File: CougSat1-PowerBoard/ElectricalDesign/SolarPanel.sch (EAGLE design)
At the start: 120 parts, among them J101 Wire Harness Connector, U1 INA199C2, U100 SPV1040, U101 SPV1040, U2 INA199C2, U3 INA199C2, U4 INA199C2, U5 AD7291, U6 AD7291, U7 AD8515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

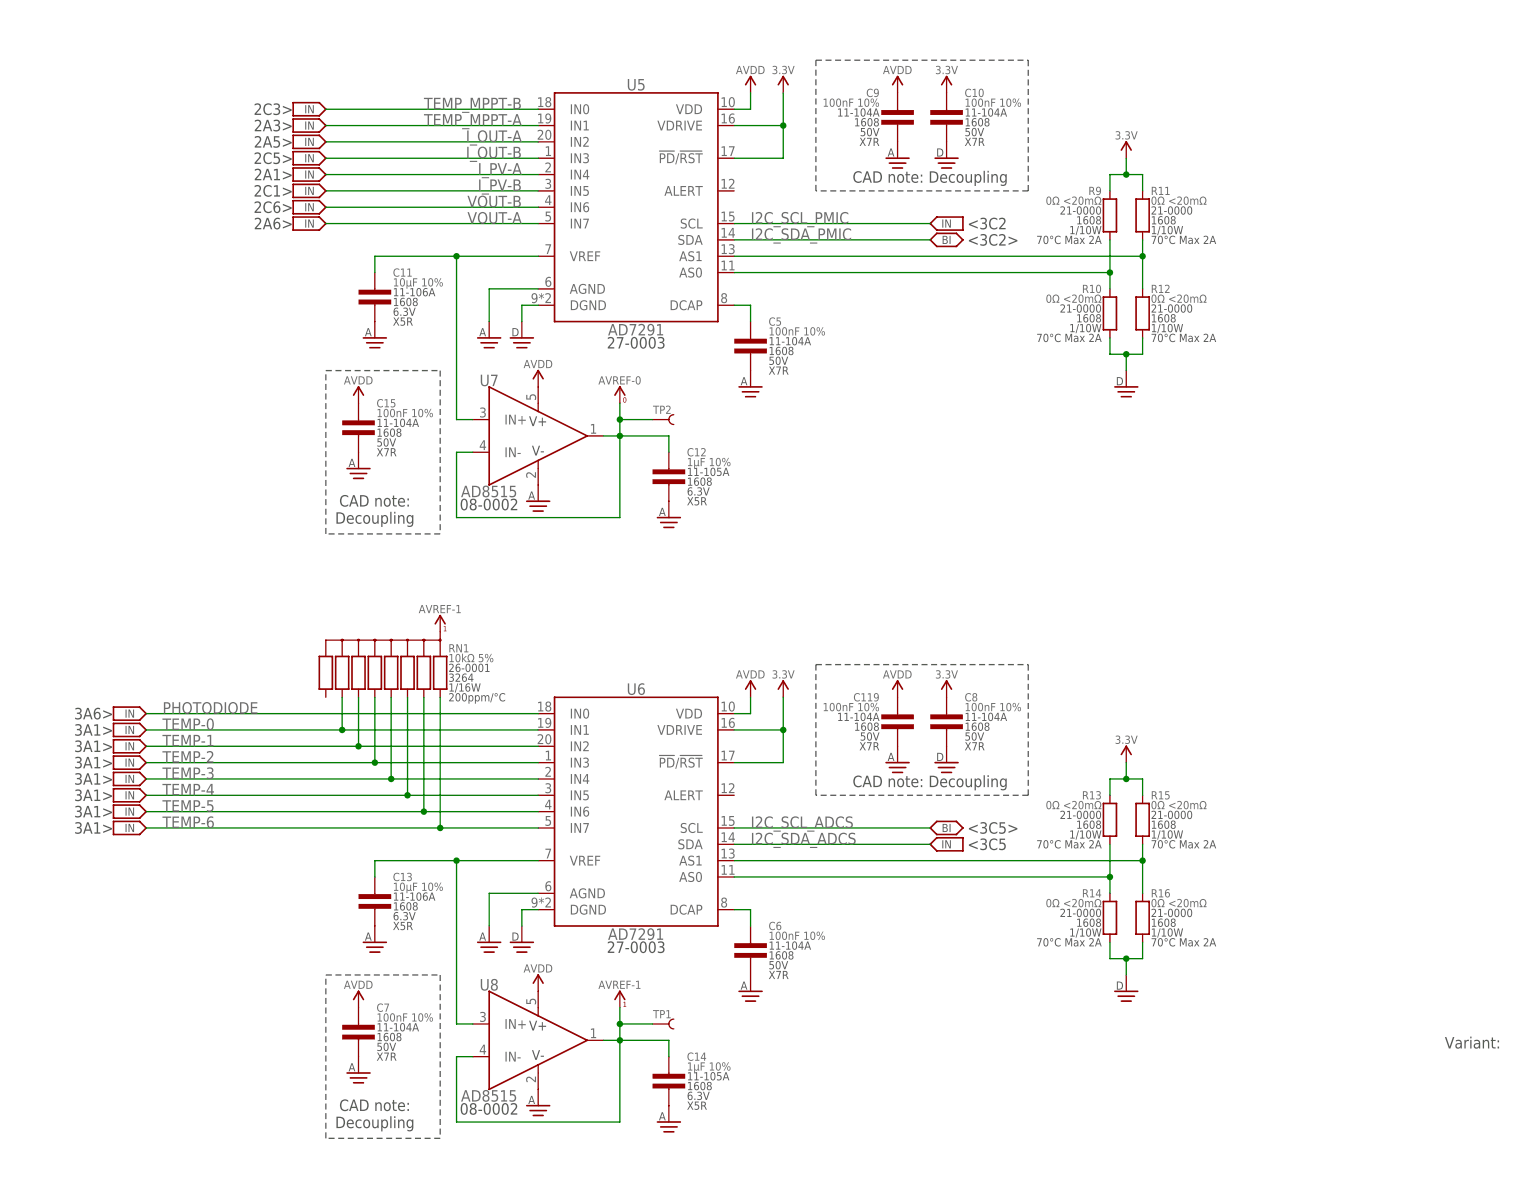
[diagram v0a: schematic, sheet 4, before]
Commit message: Stuffed addresses on variants, exported PDFs
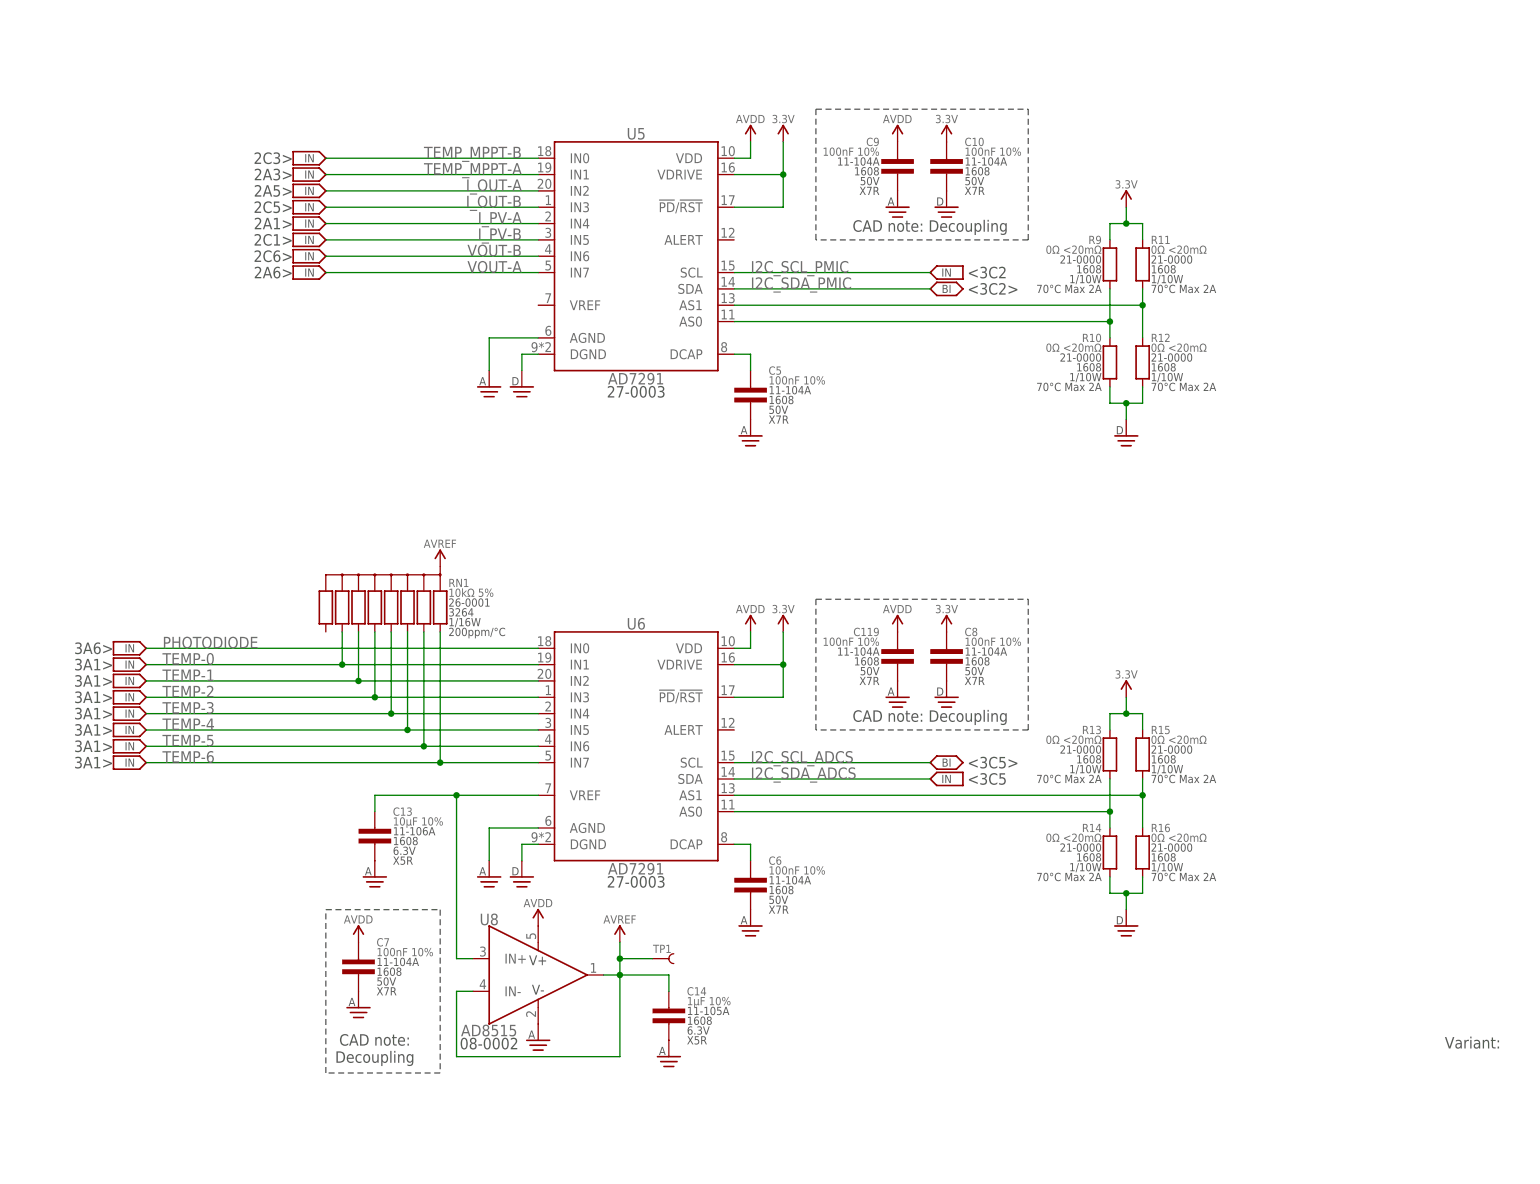
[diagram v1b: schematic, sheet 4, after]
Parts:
- removed C102, C115: 1µF 10%, CougsInSpace-Capacitors:CAP-H-1UF-1608
- removed C11: 10µF 10%, CougsInSpace-Capacitors:CAP-V-10UF-1608
- removed C12: 1µF 10%, CougsInSpace-Capacitors:CAP-V-1UF-1608
- removed C15: 100nF 10%, CougsInSpace-Capacitors:CAP-V-100NF-1608
- removed R103, R104, R127, R128: 1kΩ 0.1%, CougsInSpace-Resistors:RES-V-1K-1608
- removed R115: 150Ω 1%, CougsInSpace-Resistors:RES-V-150R-1608
- removed TP2: TEST_POINT-THT-1.0, CougsInSpace-Connectors:TEST_POINT-THT-1.0
- removed U7: AD8515, CougsInSpace-IC-Amplifiers:OPAMP-1-AD8515
- added R17: 10Ω 5%, CougsInSpace-Resistors:RES-H-10R-1608
- added R18: 33kΩ 1%, CougsInSpace-Resistors:RES-H-33K-1608
- added R19: 1kΩ 0.1%, CougsInSpace-Resistors:RES-V-1K-1608
- added U10: AD8542, CougsInSpace-IC-Amplifiers:OPAMP-2-AD8542-MSOP8
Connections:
- net AVREF-1 renamed AVREF
- net N$1 renamed PV_I_N-B
- net N$3 renamed VOUT_N-B
- net N$4 renamed VOUT_P-B
- net N$5 renamed PV_I_N-A
- net N$6 renamed PV_I_P-A
- net N$7 renamed VOUT_N-A
- net N$8 renamed VOUT_P-A
- removed net AVREF-0: C12.1, TP2.1, U7.IN-, U7.OUT
- removed net MPPT_ICTRL_N-A: C102.2, R104.1, U100.ICTRL-
- removed net MPPT_ICTRL_N-B: C115.2, R127.1, U101.ICTRL-
- removed net MPPT_ICTRL_P-A: C102.1, R103.1, U100.ICTRL+
- removed net MPPT_ICTRL_P-B: C115.1, R128.1, U101.ICTRL+
- removed net N$13: C11.1, U5.VREF, U7.IN+
- removed net N$16: R5.2-KELVIN
- new net N$1: U101.ICTRL+, U101.ICTRL-
- new net PD_AMP_FB: R18.1, R19.2, U10B.IN-
- new net PD_IN: D1.C, R17.1, U10A.IN-
- new net PD_TRANS_OUT: R17.2, U10A.OUT, U10B.IN+
- new net PV_I_P-B: R5.2-KELVIN, U1.IN+
- net AGND: now also D1.A, R19.1, U10A.IN+, U10A.V-; no longer C11.2, C12.2, C15.2, R115.1, U7.V-
- net AVDD: now also U10A.V+; no longer C15.1, D1.C, U7.V+
- net MPPT_VOUT-A: no longer R103.2
- net MPPT_VOUT-B: no longer R128.2
- net N$2: now also U100.ICTRL+, U100.ICTRL-; no longer U1.IN+
- net PHOTODIODE: now also R18.2, U10B.OUT; no longer D1.A, R115.2
- net VOUT-A: no longer R104.2
- net VOUT-B: no longer R127.2
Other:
- note added: "Note: Vmax = 1.25V"
- note removed: "CAD Note: Place facing outwards in center of board"
- note removed: "Note: Imax = 50mV Vmax = 1.25V"
- moved on the sheet: C10, C100, C117, C119, C13, C14, C5, C6, C7, C8, C9, D1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

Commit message: Fixed chematic off-sheet connectors
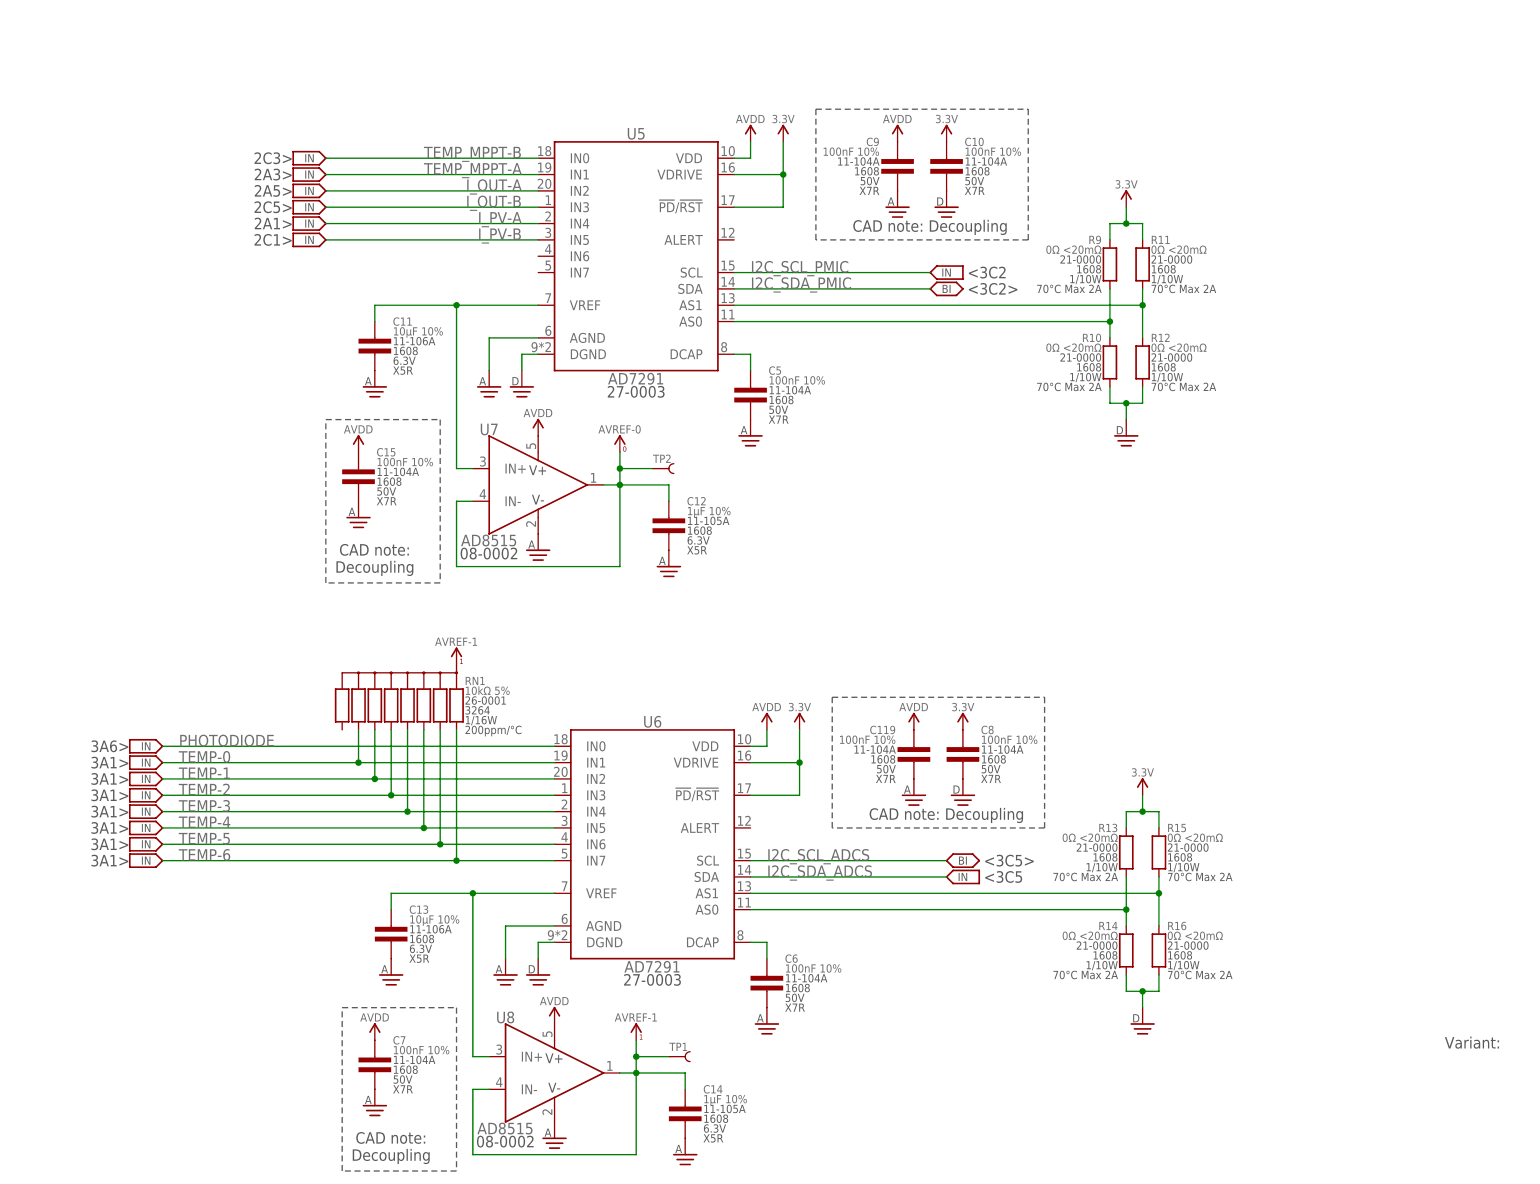
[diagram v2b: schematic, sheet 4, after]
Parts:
- added C11: 10µF 10%, CougsInSpace-Capacitors:CAP-V-10UF-1608
- added C12: 1µF 10%, CougsInSpace-Capacitors:CAP-V-1UF-1608
- added C15: 100nF 10%, CougsInSpace-Capacitors:CAP-V-100NF-1608
- added TP2: TEST_POINT-THT-1.0, CougsInSpace-Connectors:TEST_POINT-THT-1.0
- added U7: AD8515, CougsInSpace-IC-Amplifiers:OPAMP-1-AD8515
- J100: value (none) -> ADCS
- J101: value Wire Harness Connector -> EPS
- R100, R101, R110, R112: value 0Ω <20mΩ -> 2.2kΩ 1%; device CougsInSpace-Resistors:RES-V-0-1608 -> CougsInSpace-Resistors:RES-V-2.2K-1608
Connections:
- net AVREF renamed AVREF-1
- net N$10 renamed ADC_AS1-EPS
- net N$11 renamed ADC_DCAP-ADCS
- net N$12 renamed ADC_DCAP-EPS
- net N$14 renamed ADC_AS0-ADCS
- net N$15 renamed ADC_AS1-ADCS
- net N$17 renamed ADC_VREF-ADCS
- net N$9 renamed ADC_AS0-EPS
- new net ADC_VREF-EPS: C11.1, U5.VREF, U7.IN+
- new net AVREF-0: C12.1, TP2.1, U7.IN-, U7.OUT
- net AGND: now also C11.2, C12.2, C15.2, U7.V-
- net AVDD: now also C15.1, U7.V+
- net VOUT-A: no longer U5.IN7
- net VOUT-B: no longer U5.IN6
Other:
- note added: "<4C1"
- note removed: "2A6>"
- note removed: "2C6>"
- note removed: "4C1>"
- moved on the sheet: C119, C13, C14, C6, C7, C8, R13, R14, R15, R16, RN1, TP1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

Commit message: Addressed most feedback points
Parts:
- removed RT100, RT102: 68kΩ 5%, CougsInSpace-Resistors:THERMISTOR-H-68K-1608
- added R20, R21: 1kΩ 0.1%, CougsInSpace-Resistors:RES-H-1K-1608
- added R22, R23: 10kΩ 0.1%, CougsInSpace-Resistors:RES-V-10K-1608
- added RN2, RN3: 50kΩ 0.1%, CougsInSpace-Resistors:RES-H-PAIRED-50K-1616
- added RT8, RT9: 10kΩ 5%, CougsInSpace-Resistors:THERMISTOR-H-10K-1608
- added TP3, TP4: TEST_POINT-THT-1.0, CougsInSpace-Connectors:TEST_POINT-THT-1.0
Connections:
- net I_PV-A renamed PV_I-A
- net I_PV-B renamed PV_I-B
- removed net N$1: U101.ICTRL+, U101.ICTRL-
- removed net N$2: U100.ICTRL+, U100.ICTRL-
- removed net PV_IIN_P-A: C105.A, PV2.C, R7.2
- removed net PV_IIN_P-B: C113.A, PV1.C, R5.2
- new net MPPT_ICTRL-A: R20.1, U100.ICTRL+, U100.ICTRL-
- new net MPPT_ICTRL-B: R21.1, U101.ICTRL+, U101.ICTRL-
- new net PV_V-A: C105.A, PV2.C, R7.2, RN2.B1
- new net PV_V-B: C113.A, PV1.C, R5.2, RN3.B1
- new net PV_V_SENSE-A: RN2.A2, RN2.B2, U5.IN6
- new net PV_V_SENSE-B: RN3.A2, RN3.B2, U5.IN7
- net ADC_VREF-ADCS: now also TP4.1
- net ADC_VREF-EPS: now also TP3.1
- net AGND: now also RN2.A1, RN3.A1, RT8.2, RT9.2
- net AVDD: no longer RT100.1, RT102.1
- net AVREF-0: now also R22.2, R23.2
- net DGND: now also R121.2
- net MPPT_VOUT-A: now also R20.2
- net MPPT_VOUT-B: now also R21.2
- net PGND: no longer R121.2
- net TEMP_MPPT-A: now also R22.1, RT9.1; no longer RT100.2
- net TEMP_MPPT-B: now also R23.1, RT8.1; no longer RT102.2
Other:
- note added: "<4A1"
- moved on the sheet: D1, R119, R121, R125, R17, R18, R19, U10A, U10B

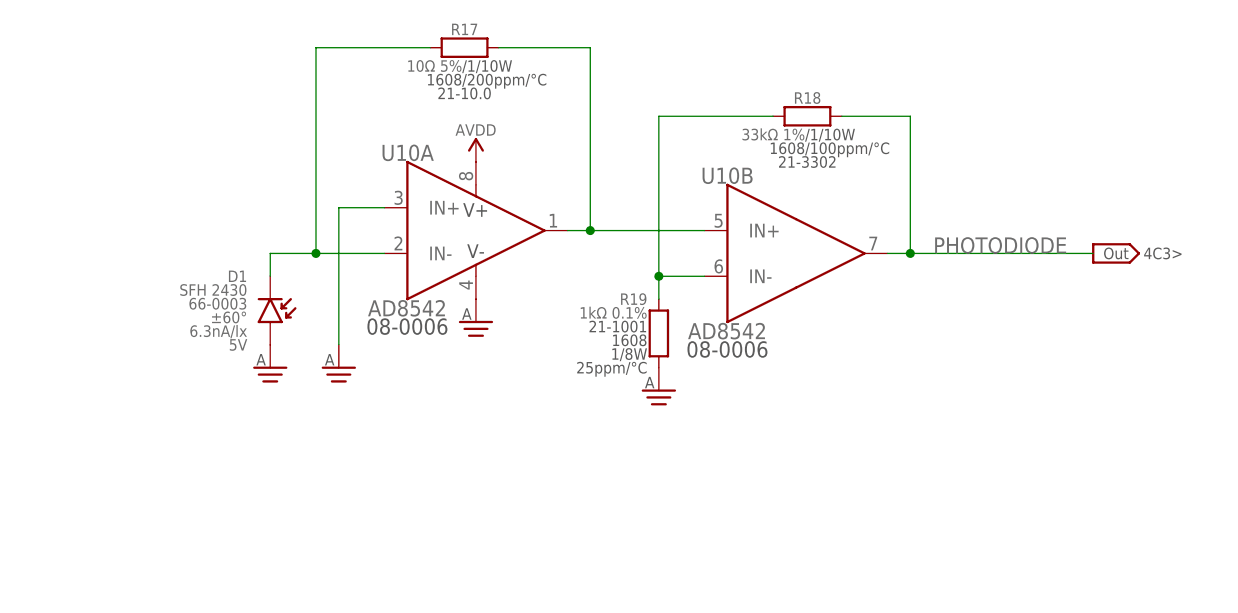
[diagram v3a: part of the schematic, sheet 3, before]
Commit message: Updated photodiode circuit
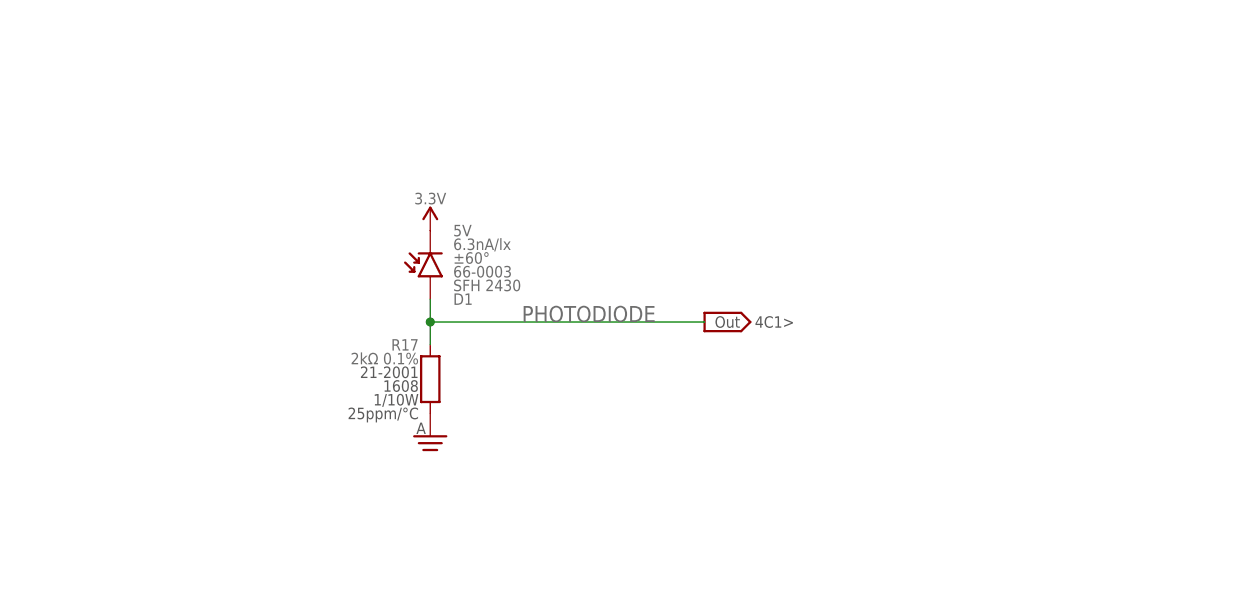
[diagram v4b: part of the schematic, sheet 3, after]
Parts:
- removed L101, L102: 10µH 20%, CougsInSpace-Coils:INDUCTOR-H-10UH-6060
- removed R18: 33kΩ 1%, CougsInSpace-Resistors:RES-H-33K-1608
- removed R19: 1kΩ 0.1%, CougsInSpace-Resistors:RES-V-1K-1608
- removed U10: AD8542, CougsInSpace-IC-Amplifiers:OPAMP-2-AD8542-MSOP8
- added L1, L2: 10µH 30%, CougsInSpace-Coils:INDUCTOR-H-10UH-SRU1038
- R17: value 10Ω 5% -> 2kΩ 0.1%; device CougsInSpace-Resistors:RES-H-10R-1608 -> CougsInSpace-Resistors:RES-V-2K-1608
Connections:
- removed net PD_AMP_FB: R18.1, R19.2, U10B.IN-
- removed net PD_IN: D1.C, R17.1, U10A.IN-
- removed net PD_TRANS_OUT: R17.2, U10A.OUT, U10B.IN+
- net 3.3V: now also D1.C
- net AGND: now also R17.1; no longer D1.A, R19.1, U10A.IN+, U10A.V-
- net AVDD: no longer U10A.V+
- net MPPT_LX-A: now also L2.2; no longer L101.2
- net MPPT_LX-B: now also L1.2; no longer L102.2
- net PHOTODIODE: now also D1.A, R17.2; no longer R18.2, U10B.OUT
- net PV_IIN_N-A: now also L2.1; no longer L101.1
- net PV_IIN_N-B: now also L1.1; no longer L102.1
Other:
- note added: "3A5>"
- note added: "4C1>"
- note removed: "3A6>"
- note removed: "4C3>"
- moved on the sheet: D1
